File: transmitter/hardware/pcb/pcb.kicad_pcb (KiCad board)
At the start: 2 copper layers, 19.1 x 33 mm, 2 parts, among them P1 digital, P2 analog

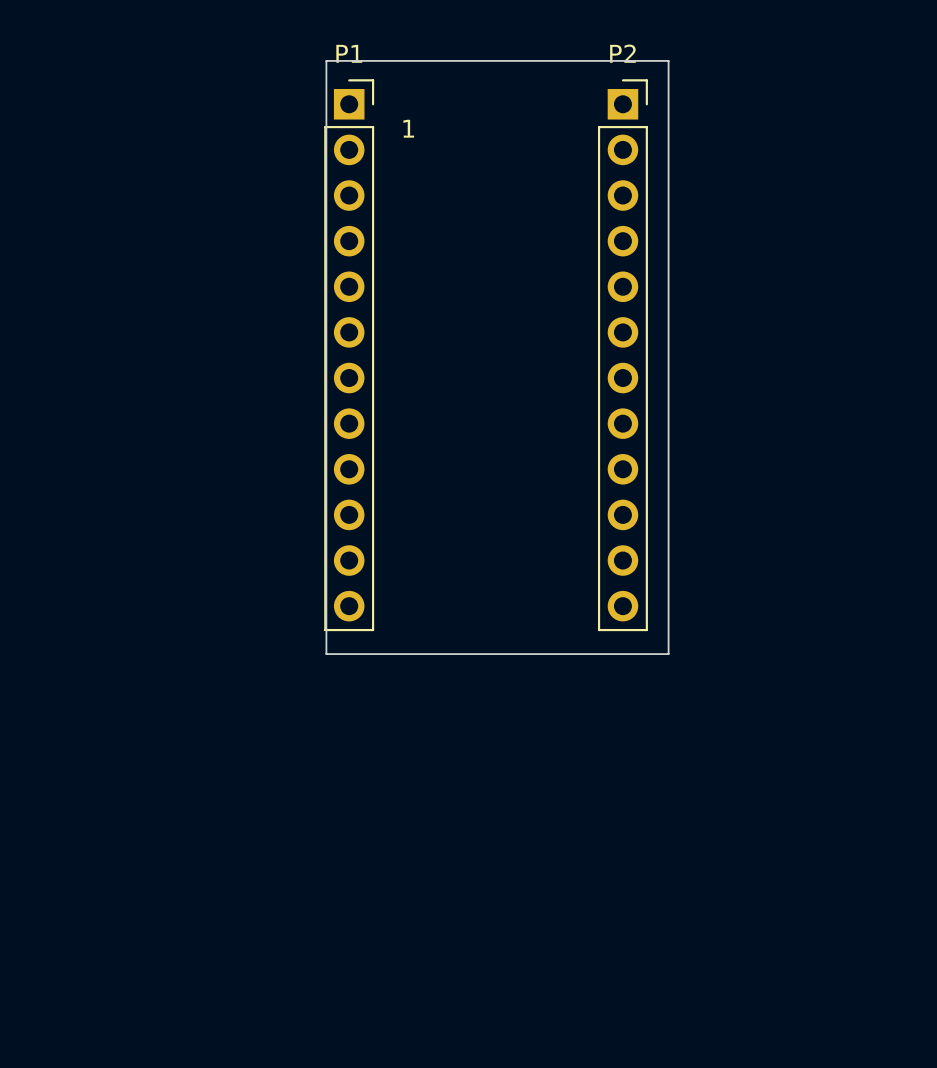
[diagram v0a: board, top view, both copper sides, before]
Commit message: Work on schematics started
Started the work on the schematics for the transmitter part
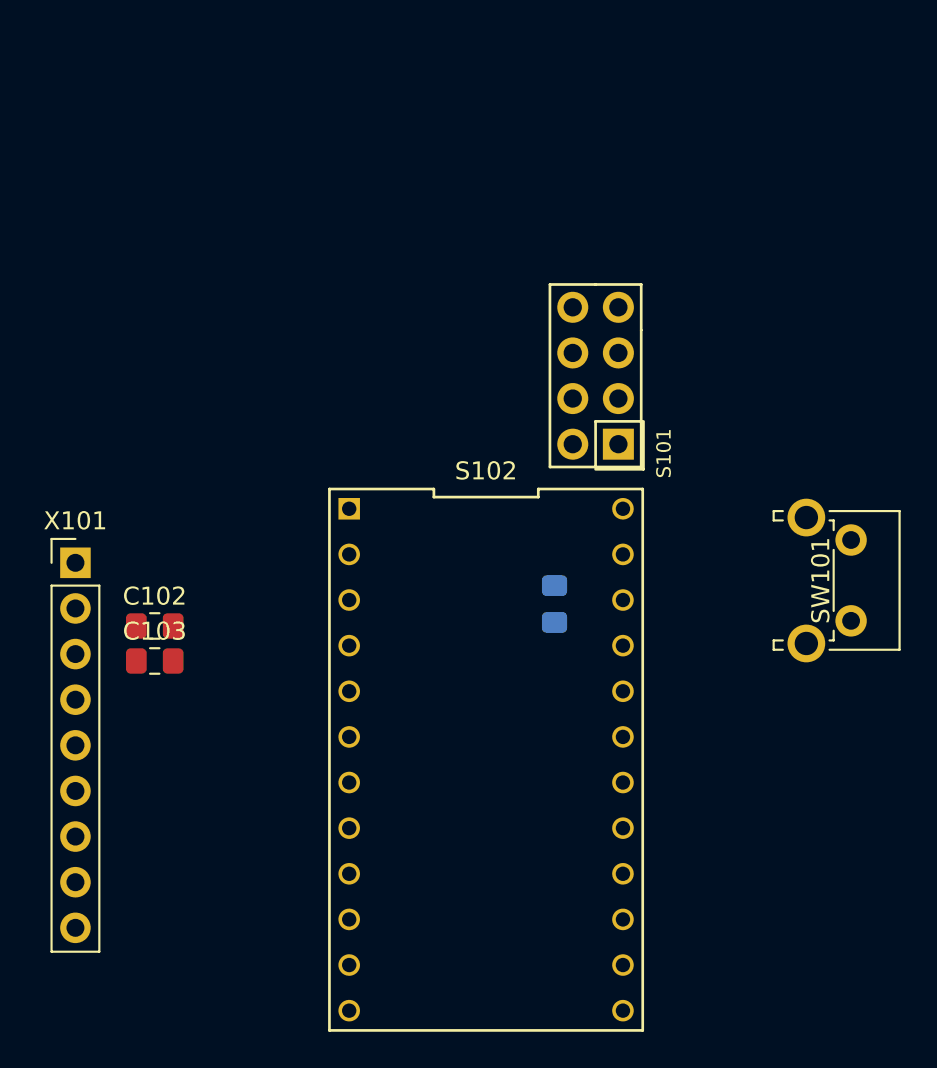
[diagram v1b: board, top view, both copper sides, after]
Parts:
- removed P1: digital, Connector_PinSocket_2.54mm:PinSocket_1x12_P2.54mm_Vertical
- removed P2: analog, Connector_PinSocket_2.54mm:PinSocket_1x12_P2.54mm_Vertical
- added C101: 100n, Capacitor_SMD:C_0805_2012Metric_Pad1.15x1.40mm_HandSolder, B.Cu at (149.9, 97.7)
- added C102: 100n, Capacitor_SMD:C_0805_2012Metric_Pad1.15x1.40mm_HandSolder, F.Cu at (127.6, 98.9)
- added C103: 100n, Capacitor_SMD:C_0805_2012Metric_Pad1.15x1.40mm_HandSolder, F.Cu at (127.6, 100.8)
- added S101: nRF24L01+, Arduino:NRF24L01, F.Cu at (154.9, 90.3)
- added S102: SparkFun_Pro_Micro, Arduino:DIP-24_600, F.Cu at (146.1, 105.5)
- added SW101: ~RST, Button_Switch_THT:SW_Tactile_SPST_Angled_PTS645Vx39-2LFS, F.Cu at (166.4, 94.1)
- added X101: Display, Connector_PinHeader_2.54mm:PinHeader_1x09_P2.54mm_Vertical, F.Cu at (123.2, 95.4)
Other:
- board outline removed
- board text removed: "1"

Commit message: WIP commit
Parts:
- added C104: 100n, Capacitor_SMD:C_0805_2012Metric_Pad1.15x1.40mm_HandSolder, F.Cu at (186.5, 85.7)
- added C105: 10u, Capacitor_SMD:C_1206_3216Metric, F.Cu at (197.7, 71.0)
- added C106: 100n, Capacitor_SMD:C_0805_2012Metric_Pad1.15x1.40mm_HandSolder, F.Cu at (197.3, 73.1)
- added C107: 100n, Capacitor_SMD:C_0805_2012Metric_Pad1.15x1.40mm_HandSolder, F.Cu at (146.9, 100.8)
- added C108: 100n, Capacitor_SMD:C_0805_2012Metric_Pad1.15x1.40mm_HandSolder, F.Cu at (197.3, 75.1)
- added C201: 10n, Capacitor_SMD:C_0603_1608Metric, F.Cu at (226.1, 62.4)
- added C202: 100n, Capacitor_SMD:C_0603_1608Metric, F.Cu at (224.2, 80.8)
- added C203: 15p, Capacitor_SMD:C_0603_1608Metric, F.Cu at (232.4, 80.8)
- added C204: 15p, Capacitor_SMD:C_0603_1608Metric, F.Cu at (226.1, 80.8)
- added C205: 1u, Capacitor_SMD:C_0805_2012Metric_Pad1.15x1.40mm_HandSolder, F.Cu at (219.7, 70.6)
- added C206: 100n, Capacitor_SMD:C_0603_1608Metric, F.Cu at (233.0, 62.4)
- added C207: 100n, Capacitor_SMD:C_0603_1608Metric, F.Cu at (220.3, 67.4)
- added C208: 100n, Capacitor_SMD:C_0603_1608Metric, F.Cu at (224.2, 62.4)
- added C209: 100n, Capacitor_SMD:C_0603_1608Metric, F.Cu at (236.9, 74.4)
- added P101: TestPoint_Alt, TestPoint:TestPoint_Pad_D1.0mm, F.Cu at (185.6, 92.8)
- added P102: TestPoint_Alt, TestPoint:TestPoint_Pad_D1.0mm, F.Cu at (163.0, 90.0)
- added P103: TestPoint_Alt, TestPoint:TestPoint_Pad_D1.0mm, F.Cu at (185.6, 90.7)
- added P104: TestPoint_Alt, TestPoint:TestPoint_Pad_D1.0mm, F.Cu at (192.4, 85.4)
- added P105: TestPoint_Alt, TestPoint:TestPoint_Pad_D1.0mm, F.Cu at (168.9, 90.8)
- added P106: TestPoint_Alt, TestPoint:TestPoint_Pad_D1.0mm, F.Cu at (166.6, 100.0)
- added P107: TestPoint_Alt, TestPoint:TestPoint_Pad_D1.0mm, F.Cu at (166.6, 102.0)
- added P108: TestPoint_Alt, TestPoint:TestPoint_Pad_D1.0mm, F.Cu at (163.0, 94.1)
- added P109: TestPoint_Alt, TestPoint:TestPoint_Pad_D1.0mm, F.Cu at (178.5, 96.9)
- added P110: TestPoint_Alt, TestPoint:TestPoint_Pad_D1.0mm, F.Cu at (189.4, 86.3)
- added P111: TestPoint_Alt, TestPoint:TestPoint_Pad_D1.0mm, F.Cu at (192.4, 83.4)
- added P112: TestPoint_Alt, TestPoint:TestPoint_Pad_D1.0mm, F.Cu at (168.9, 86.7)
- added P113: TestPoint_Alt, TestPoint:TestPoint_Pad_D1.0mm, F.Cu at (166.6, 97.9)
- added P114: TestPoint_Alt, TestPoint:TestPoint_Pad_D1.0mm, F.Cu at (168.9, 88.7)
- added P115: TestPoint_Alt, TestPoint:TestPoint_Pad_D1.0mm, F.Cu at (188.6, 88.3)
- added P116: TestPoint_Alt, TestPoint:TestPoint_Pad_D1.0mm, F.Cu at (196.5, 82.1)
- added P117: TestPoint_Alt, TestPoint:TestPoint_Pad_D1.0mm, F.Cu at (198.2, 80.1)
- added P118: TestPoint_Alt, TestPoint:TestPoint_Pad_D1.0mm, F.Cu at (178.5, 101.0)
- added P119: TestPoint_Alt, TestPoint:TestPoint_Pad_D1.0mm, F.Cu at (181.5, 93.9)
- added P120: TestPoint_Alt, TestPoint:TestPoint_Pad_D1.0mm, F.Cu at (163.0, 92.1)
- added P121: TestPoint_Alt, TestPoint:TestPoint_Pad_D1.0mm, F.Cu at (183.6, 95.5)
- added P122: TestPoint_Alt, TestPoint:TestPoint_Pad_D1.0mm, F.Cu at (180.6, 99.0)
- added P123: TestPoint_Alt, TestPoint:TestPoint_Pad_D1.0mm, F.Cu at (194.4, 85.4)
- added P124: TestPoint_Alt, TestPoint:TestPoint_Pad_D1.0mm, F.Cu at (196.2, 80.1)
- added P125: TestPoint_Alt, TestPoint:TestPoint_Pad_D1.0mm, F.Cu at (183.6, 93.5)
- added P126: TestPoint_Alt, TestPoint:TestPoint_Pad_D1.0mm, F.Cu at (178.5, 99.0)
- added P127: TestPoint_Alt, TestPoint:TestPoint_Pad_D1.0mm, F.Cu at (180.6, 96.9)
- added P128: TestPoint_Alt, TestPoint:TestPoint_Pad_D1.0mm, F.Cu at (194.4, 83.4)
- added P129: TestPoint_Alt, TestPoint:TestPoint_Pad_D1.0mm, F.Cu at (187.7, 90.7)
- added P130: TestPoint_Alt, TestPoint:TestPoint_Pad_D1.0mm, F.Cu at (190.7, 88.3)
- added P131: TestPoint_Alt, TestPoint:TestPoint_Pad_D1.0mm, F.Cu at (213.4, 88.4)
- added P201: TestPoint_Alt, TestPoint:TestPoint_Pad_D1.0mm, F.Cu at (227.3, 62.4)
- added P202: TestPoint_Alt, TestPoint:TestPoint_Pad_D1.0mm, F.Cu at (230.5, 78.9)
- added P203: TestPoint_Alt, TestPoint:TestPoint_Pad_D1.0mm, F.Cu at (228.0, 78.9)
- added P204: TestPoint_Alt, TestPoint:TestPoint_Pad_D1.0mm, F.Cu at (217.8, 71.2)
- added Q101: BC847, Package_TO_SOT_SMD:SOT-23, F.Cu at (159.7, 99.5)
- added Q201: 16M, Crystal:Crystal_SMD_TXC_7M-4Pin_3.2x2.5mm, F.Cu at (229.2, 81.4)
- added R101: 22R, Resistor_SMD:R_0603_1608Metric, F.Cu at (189.9, 84.5)
- added R102: 22R, Resistor_SMD:R_0603_1608Metric, F.Cu at (179.0, 95.2)
- added R103: 2k, Resistor_SMD:R_0603_1608Metric, F.Cu at (182.6, 91.7)
- added R104: 1k, Resistor_SMD:R_0603_1608Metric, F.Cu at (179.0, 93.7)
- added R105: 2.9k, Resistor_SMD:R_0603_1608Metric, F.Cu at (189.8, 83.0)
- added R106: 1k, Resistor_SMD:R_0603_1608Metric, F.Cu at (193.4, 81.6)
- added R107: 330R, Resistor_SMD:R_0603_1608Metric, F.Cu at (197.2, 76.8)
- added R108: 0R, Resistor_SMD:R_0603_1608Metric, F.Cu at (186.1, 87.5)
- added R109: 6.8k, Resistor_SMD:R_0603_1608Metric, F.Cu at (186.1, 89.0)
- added R110: 1.6k, Resistor_SMD:R_0603_1608Metric, F.Cu at (159.5, 102.0)
- added R111: 620R, Resistor_SMD:R_0603_1608Metric, F.Cu at (146.6, 102.6)
- added R112: 150R, Resistor_SMD:R_0603_1608Metric, F.Cu at (197.2, 78.3)
- added R201: 1k, Resistor_SMD:R_0603_1608Metric, F.Cu at (225.4, 78.2)
- added R202: 100R, Resistor_SMD:R_0603_1608Metric, F.Cu at (222.2, 62.4)
- added RN101: 1k, Resistor_THT:R_Array_SIP9, F.Cu at (142.2, 87.3)
- added S103: NRF24L01_Breakout, RF_Module:nRF24L01_Breakout, F.Cu at (142.2, 72.1)
- added S201: ATmega32U4-AU, Package_QFP:TQFP-44_10x10mm_P0.8mm, F.Cu at (228.6, 70.6)
- added U101: AMS1117-3.3, Package_TO_SOT_SMD:SOT-223-3_TabPin2, F.Cu at (153.5, 99.8)
- added X102: SW1, Connector_PinHeader_2.54mm:PinHeader_1x02_P2.54mm_Vertical, F.Cu at (163.8, 98.7)
- added X103: SW2, Connector_PinHeader_2.54mm:PinHeader_1x02_P2.54mm_Vertical, F.Cu at (193.6, 71.7)
- added X104: SW3, Connector_PinHeader_2.54mm:PinHeader_1x02_P2.54mm_Vertical, F.Cu at (179.1, 86.6)
- added X105: SW4, Connector_PinHeader_2.54mm:PinHeader_1x02_P2.54mm_Vertical, F.Cu at (190.1, 77.9)
- added X106: SW5, Connector_PinHeader_2.54mm:PinHeader_1x02_P2.54mm_Vertical, F.Cu at (189.9, 71.7)
- added X107: SW6, Connector_PinHeader_2.54mm:PinHeader_1x02_P2.54mm_Vertical, F.Cu at (182.8, 86.6)
- added X108: SW7, Connector_PinHeader_2.54mm:PinHeader_1x02_P2.54mm_Vertical, F.Cu at (186.4, 80.4)
- added X109: SW8, Connector_PinHeader_2.54mm:PinHeader_1x02_P2.54mm_Vertical, F.Cu at (182.8, 80.4)
- added X110: PWR_5V, Connector_PinHeader_2.54mm:PinHeader_1x02_P2.54mm_Vertical, F.Cu at (179.1, 80.4)
- added X111: UART, Connector_PinHeader_2.54mm:PinHeader_1x04_P2.54mm_Vertical, F.Cu at (166.1, 87.5)
- added X112: gimbal_left_h, Connector_PinSocket_2.54mm:PinSocket_1x03_P2.54mm_Vertical, F.Cu at (179.1, 71.7)
- added X113: gimbal_left_v, Connector_PinSocket_2.54mm:PinSocket_1x03_P2.54mm_Vertical, F.Cu at (182.7, 71.7)
- added X114: gimbal_right_h, Connector_PinSocket_2.54mm:PinSocket_1x03_P2.54mm_Vertical, F.Cu at (186.3, 71.7)
- added X115: gimbal_right_v, Connector_PinSocket_2.54mm:PinSocket_1x03_P2.54mm_Vertical, F.Cu at (160.2, 90.8)
- added X116: analog trimm buttons, Connector_PinHeader_2.54mm:PinHeader_1x09_P2.54mm_Vertical, F.Cu at (171.8, 71.7)
- added X117: Display, Connector_PinHeader_2.54mm:PinHeader_1x09_P2.54mm_Vertical, F.Cu at (175.5, 71.7)
- added X201: AVR-ISP-6, Connector_PinHeader_2.54mm:PinHeader_2x03_P2.54mm_Vertical, F.Cu at (214.6, 75.1)
- C101: value 100n -> 10u; footprint Capacitor_SMD:C_0805_2012Metric_Pad1.15x1.40mm_HandSolder -> Capacitor_SMD:C_1206_3216Metric; moved to F.Cu
- S101: value nRF24L01+ -> 74HC165; footprint Arduino:NRF24L01 -> Package_SO:SOIC-16_3.9x9.9mm_P1.27mm
- S102: value SparkFun_Pro_Micro -> 74AHC1G125; footprint Arduino:DIP-24_600 -> Package_TO_SOT_SMD:SOT-353_SC-70-5
- X101: value Display -> USB_B_Micro; footprint Connector_PinHeader_2.54mm:PinHeader_1x09_P2.54mm_Vertical -> Connector_USB:USB_Micro-B_GCT_USB3076-30-A
- moved C103 70.3 mm to (193.8, 77.0)
- moved S102 54.2 mm to (193.5, 79.4)
- moved C102 52.1 mm to (179.2, 91.9)
- moved X101 30.8 mm to (153.7, 91.7)
- moved S101 11.0 mm to (144.8, 94.4), turned to 0 degrees
- moved C101 7.83 mm to (142.8, 101.0), turned to 0 degrees
- moved SW101 5.43 mm to (170.4, 97.7), turned to 0 degrees
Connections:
- C102 pad 1: +3V3 -> +5V
- S101 pad 1: GND -> /PE_LATCH
- S101 pad 2: +3V3 -> /SCK
- S101 pad 3: /CE -> Net-(P105-Pad1)
- S101 pad 4: /~CS1 -> Net-(P106-Pad1)
- S101 pad 5: /SCK -> Net-(P107-Pad1)
- S101 pad 6: /MOSI -> Net-(P108-Pad1)
- S101 pad 7: /MISO -> Net-(S101-Pad7)
- S101 pad 8: /IRQ -> GND
- S102 pad 1: /~RST -> /~CE3
- S102 pad 2: /BLEN -> Net-(P116-Pad1)
- S102 pad 4: GND -> /MISO
- S102 pad 5: /IRQ -> +5V
- SW101 pad 1: GND -> /~RST
- SW101 pad 2: Net-(S102-Pad22) -> GND
- X101 pad 1: GND -> /VBUS
- X101 pad 2: +5V -> Net-(R102-Pad2)
- X101 pad 3: /~RST -> Net-(R101-Pad2)
- X101 pad 4: /DC -> Net-(X101-Pad4)
- X101 pad 5: /MOSI -> GND
- X101 pad 6: /SCK -> GND
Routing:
- net GND: track 0.00 -> 31.9 mm
- net /MOSI: track 0.00 -> 11.3 mm
- net /SCK: track 0.00 -> 8.48 mm
- net /MISO: track 0.00 -> 8.45 mm
- net Net-(C208-Pad1): track 0.00 -> 8.26 mm
- net Net-(C203-Pad1): track 0.00 -> 7.62 mm
- net Net-(C204-Pad1): track 0.00 -> 6.70 mm
- net Net-(C205-Pad1): track 0.00 -> 5.68 mm
- net +5V: track 0.00 -> 5.65 mm
- net /~RST: track 0.00 -> 4.19 mm
- net Net-(C201-Pad1): track 0.00 -> 3.42 mm

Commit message: WIP
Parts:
- added C109: 10u, Capacitor_SMD:C_1206_3216Metric, F.Cu at (167.4, 89.0)
- added C110: 10u, Capacitor_SMD:C_1206_3216Metric, F.Cu at (182.9, 97.7)
- added C111: 10u, Capacitor_SMD:C_1206_3216Metric, F.Cu at (123.6, 81.6)
- added C112: 100n, Capacitor_SMD:C_0805_2012Metric_Pad1.15x1.40mm_HandSolder, F.Cu at (127.8, 83.4)
- added C113: 100n, Capacitor_SMD:C_0805_2012Metric_Pad1.15x1.40mm_HandSolder, F.Cu at (127.8, 81.4)
- added C114: 100n, Capacitor_SMD:C_0805_2012Metric_Pad1.15x1.40mm_HandSolder, F.Cu at (123.2, 83.7)
- added D101: green, LED_THT:LED_D3.0mm, F.Cu at (239.7, 102.2)
- added D102: red, LED_THT:LED_D3.0mm, F.Cu at (235.3, 102.2)
- added P132: TestPoint_Alt, TestPoint:TestPoint_Pad_D1.0mm, F.Cu at (201.3, 86.4)
- added P133: TestPoint_Alt, TestPoint:TestPoint_Pad_D1.0mm, F.Cu at (192.4, 94.2)
- added P134: TestPoint_Alt, TestPoint:TestPoint_Pad_D1.0mm, F.Cu at (198.2, 87.9)
- added P135: TestPoint_Alt, TestPoint:TestPoint_Pad_D1.0mm, F.Cu at (184.1, 99.7)
- added P136: TestPoint_Alt, TestPoint:TestPoint_Pad_D1.0mm, F.Cu at (195.2, 90.5)
- added P137: TestPoint_Alt, TestPoint:TestPoint_Pad_D1.0mm, F.Cu at (211.5, 74.7)
- added P138: TestPoint_Alt, TestPoint:TestPoint_Pad_D1.0mm, F.Cu at (174.6, 83.5)
- added P139: TestPoint_Alt, TestPoint:TestPoint_Pad_D1.0mm, F.Cu at (119.9, 85.8)
- added P140: TestPoint_Alt, TestPoint:TestPoint_Pad_D1.0mm, F.Cu at (117.9, 87.9)
- added P141: TestPoint_Alt, TestPoint:TestPoint_Pad_D1.0mm, F.Cu at (117.9, 85.8)
- added P142: TestPoint_Alt, TestPoint:TestPoint_Pad_D1.0mm, F.Cu at (119.9, 87.9)
- added P143: TestPoint_Alt, TestPoint:TestPoint_Pad_D1.0mm, F.Cu at (122.0, 87.2)
- added P144: TestPoint_Alt, TestPoint:TestPoint_Pad_D1.0mm, F.Cu at (114.9, 89.9)
- added P145: TestPoint_Alt, TestPoint:TestPoint_Pad_D1.0mm, F.Cu at (116.9, 89.9)
- added R113: 1.6k, Resistor_SMD:R_0603_1608Metric, F.Cu at (189.9, 91.9)
- added R114: 1k, Resistor_SMD:R_0603_1608Metric, F.Cu at (195.7, 85.7)
- added R115: 620R, Resistor_SMD:R_0603_1608Metric, F.Cu at (195.7, 88.7)
- added R116: 330R, Resistor_SMD:R_0603_1608Metric, F.Cu at (202.6, 79.9)
- added R117: 150R, Resistor_SMD:R_0603_1608Metric, F.Cu at (181.6, 101.4)
- added R118: 0R, Resistor_SMD:R_0603_1608Metric, F.Cu at (115.3, 87.0)
- added R119: 1k, Resistor_SMD:R_0603_1608Metric, F.Cu at (122.8, 85.5)
- added S104: 74AHC1G125, Package_TO_SOT_SMD:SOT-353_SC-70-5, F.Cu at (177.3, 93.8)
- added S105: 74HC165, Package_SO:SOIC-16_3.9x9.9mm_P1.27mm, F.Cu at (117.6, 79.5)
- added SW102: ~RST, Button_Switch_THT:SW_Tactile_SPST_Angled_PTS645Vx39-2LFS, F.Cu at (201.6, 68.5)
- added X118: analog_in1, Connector_Molex:Molex_KK-254_AE-6410-05A_1x05_P2.54mm_Vertical, F.Cu at (144.5, 126.3)
- added X119: SW5, Connector_PinHeader_2.54mm:PinHeader_1x02_P2.54mm_Vertical, F.Cu at (126.8, 76.1)
- added X120: SW6, Connector_PinHeader_2.54mm:PinHeader_1x02_P2.54mm_Vertical, F.Cu at (123.1, 76.1)
- added X121: SW7, Connector_PinHeader_2.54mm:PinHeader_1x02_P2.54mm_Vertical, F.Cu at (134.1, 76.1)
- added X122: analog trimm buttons, Connector_PinHeader_2.54mm:PinHeader_1x09_P2.54mm_Vertical, F.Cu at (112.0, 76.1)
- added X123: SW8, Connector_PinHeader_2.54mm:PinHeader_1x02_P2.54mm_Vertical, F.Cu at (130.4, 76.1)
- C104, C106: value 100n -> 10u; footprint Capacitor_SMD:C_0805_2012Metric_Pad1.15x1.40mm_HandSolder -> Capacitor_SMD:C_1206_3216Metric
- C105: value 10u -> 100n; footprint Capacitor_SMD:C_1206_3216Metric -> Capacitor_SMD:C_0805_2012Metric_Pad1.15x1.40mm_HandSolder; moved to B.Cu
- C201: value 10n -> 100n
- C203, C204: value 15p -> 100n
- C205: value 1u -> 100n; footprint Capacitor_SMD:C_0805_2012Metric_Pad1.15x1.40mm_HandSolder -> Capacitor_SMD:C_0603_1608Metric
- C206, C207: value 100n -> 15p
- C208: value 100n -> 10n
- C209: value 100n -> 1u; footprint Capacitor_SMD:C_0603_1608Metric -> Capacitor_SMD:C_0805_2012Metric_Pad1.15x1.40mm_HandSolder
- Q201: footprint Crystal:Crystal_SMD_TXC_7M-4Pin_3.2x2.5mm -> Crystal:Crystal_SMD_HC49-SD
- R101: value 22R -> n.b
- R102: value 22R -> 1k
- R103: value 2k -> 1k
- R104: value 1k -> 1,2k
- R105: value 2.9k -> 0R
- R106: value 1k -> 4,7k
- R107: value 330R -> 4,7k
- R108: value 0R -> 22R
- R109: value 6.8k -> 22R
- R110: value 1.6k -> 2k
- R111: value 620R -> 6.8k
- R112: value 150R -> 2.9k
- R201: value 1k -> 100R
- R202: value 100R -> 1k
- S101: value 74HC165 -> Step-Up; footprint Package_SO:SOIC-16_3.9x9.9mm_P1.27mm -> Package_SO:SOIC-8-1EP_3.9x4.9mm_P1.27mm_EP2.35x2.35mm
- S102: value 74AHC1G125 -> NRF24L01_Breakout; footprint Package_TO_SOT_SMD:SOT-353_SC-70-5 -> RF_Module:nRF24L01_Breakout
- S103: value NRF24L01_Breakout -> TP4056; footprint RF_Module:nRF24L01_Breakout -> Package_SO:SOIC-8-1EP_3.9x4.9mm_P1.27mm_EP2.35x2.35mm
- SW101: value ~RST -> Power; footprint Button_Switch_THT:SW_Tactile_SPST_Angled_PTS645Vx39-2LFS -> Module:SW_Graupner_JS202011AQN_DPDT_Angled
- X101: value USB_B_Micro -> PWR_5V; footprint Connector_USB:USB_Micro-B_GCT_USB3076-30-A -> Connector_PinHeader_2.54mm:PinHeader_1x03_P2.54mm_Vertical
- X102: value SW1 -> Charger; footprint Connector_PinHeader_2.54mm:PinHeader_1x02_P2.54mm_Vertical -> Connector_BarrelJack:BarrelJack_Horizontal
- X103: value SW2 -> Display; footprint Connector_PinHeader_2.54mm:PinHeader_1x02_P2.54mm_Vertical -> Connector_PinHeader_2.54mm:PinHeader_1x09_P2.54mm_Vertical
- X104: value SW3 -> I2C; footprint Connector_PinHeader_2.54mm:PinHeader_1x02_P2.54mm_Vertical -> Connector_PinHeader_2.54mm:PinHeader_1x04_P2.54mm_Vertical
- X105: value SW4 -> UART; footprint Connector_PinHeader_2.54mm:PinHeader_1x02_P2.54mm_Vertical -> Connector_PinHeader_2.54mm:PinHeader_1x04_P2.54mm_Vertical
- X106: value SW5 -> USB_B_Micro; footprint Connector_PinHeader_2.54mm:PinHeader_1x02_P2.54mm_Vertical -> Connector_USB:USB_Micro-B_GCT_USB3076-30-A
- X107: value SW6 -> analog_in2; footprint Connector_PinHeader_2.54mm:PinHeader_1x02_P2.54mm_Vertical -> Connector_Molex:Molex_KK-254_AE-6410-05A_1x05_P2.54mm_Vertical
- X108: value SW7 -> analog_in3; footprint Connector_PinHeader_2.54mm:PinHeader_1x02_P2.54mm_Vertical -> Connector_Molex:Molex_KK-254_AE-6410-05A_1x05_P2.54mm_Vertical
- X109: value SW8 -> gimbal_left_h; footprint Connector_PinHeader_2.54mm:PinHeader_1x02_P2.54mm_Vertical -> Connector_Molex:Molex_KK-254_AE-6410-05A_1x05_P2.54mm_Vertical
- X110: value PWR_5V -> analog_in4; footprint Connector_PinHeader_2.54mm:PinHeader_1x02_P2.54mm_Vertical -> Connector_Molex:Molex_KK-254_AE-6410-05A_1x05_P2.54mm_Vertical
- X111: value UART -> gimbal_left_v; footprint Connector_PinHeader_2.54mm:PinHeader_1x04_P2.54mm_Vertical -> Connector_Molex:Molex_KK-254_AE-6410-05A_1x05_P2.54mm_Vertical
- X112: value gimbal_left_h -> gimbal_right_h; footprint Connector_PinSocket_2.54mm:PinSocket_1x03_P2.54mm_Vertical -> Connector_Molex:Molex_KK-254_AE-6410-05A_1x05_P2.54mm_Vertical
- X113: value gimbal_left_v -> SW1; footprint Connector_PinSocket_2.54mm:PinSocket_1x03_P2.54mm_Vertical -> Connector_PinHeader_2.54mm:PinHeader_1x02_P2.54mm_Vertical
- X114: value gimbal_right_h -> SW2; footprint Connector_PinSocket_2.54mm:PinSocket_1x03_P2.54mm_Vertical -> Connector_PinHeader_2.54mm:PinHeader_1x02_P2.54mm_Vertical
- X115: footprint Connector_PinSocket_2.54mm:PinSocket_1x03_P2.54mm_Vertical -> Connector_Molex:Molex_KK-254_AE-6410-05A_1x05_P2.54mm_Vertical
- X116: value analog trimm buttons -> SW3; footprint Connector_PinHeader_2.54mm:PinHeader_1x09_P2.54mm_Vertical -> Connector_PinHeader_2.54mm:PinHeader_1x02_P2.54mm_Vertical
- X117: value Display -> SW4; footprint Connector_PinHeader_2.54mm:PinHeader_1x09_P2.54mm_Vertical -> Connector_PinHeader_2.54mm:PinHeader_1x02_P2.54mm_Vertical
- moved S102 114.0 mm to (95.6, 137.8), turned to 180 degrees
- moved S101 85.7 mm to (229.6, 106.6)
- moved P108 76.5 mm to (238.5, 106.6)
- moved C105 75.7 mm to (219.4, 143.5)
- moved X101 68.4 mm to (213.1, 125.7)
- moved S103 68.0 mm to (210.3, 72.2)
- moved P106 67.6 mm to (234.0, 106.0)
- moved X102 66.4 mm to (216.2, 139.6), turned to 180 degrees
- moved P105 64.7 mm to (211.4, 139.5)
- moved R102 61.5 mm to (239.7, 104.7), turned to 270 degrees
- moved SW101 59.5 mm to (195.7, 151.6), turned to 180 degrees
- moved X112 58.9 mm to (157.2, 126.3), turned to 90 degrees
- moved C106 56.5 mm to (209.9, 128.2), turned to 270 degrees
- moved R103 54.3 mm to (235.3, 104.7), turned to 270 degrees
- moved P113 48.8 mm to (211.5, 78.8)
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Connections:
- C103 pad 1: +5V -> +3V3
- C106 pad 1: +5V -> Net-(C106-Pad1)
- C107 pad 1: +3V3 -> Net-(C106-Pad1)
- C201 pad 1: Net-(C201-Pad1) -> +5V
- C202 pad 1: /~RST -> +5V
- C204 pad 1: Net-(C204-Pad1) -> Net-(C203-Pad1)
- C205 pad 1: Net-(C205-Pad1) -> /~RST
- C206 pad 1: +5V -> Net-(C206-Pad1)
- C207 pad 1: +5V -> Net-(C207-Pad1)
- C209 pad 1: Net-(C208-Pad1) -> Net-(C209-Pad1)
- P101 pad 1: Net-(P101-Pad1) -> +3V3
- P102 pad 1: Net-(P102-Pad1) -> Net-(C106-Pad1)
- P103 pad 1: Net-(P103-Pad1) -> +BATT
- P104 pad 1: Net-(P104-Pad1) -> GND
- P105 pad 1: Net-(P105-Pad1) -> ~CS_nRF24
- P106 pad 1: Net-(P106-Pad1) -> CE
- P107 pad 1: Net-(P107-Pad1) -> +5C
- P109 pad 1: GND -> /NTC
- P110 pad 1: +5V -> Net-(P110-Pad1)
- P111 pad 1: /~RST -> Net-(P111-Pad1)
- P112 pad 1: /VBUS -> ~LCD_RST
- P113 pad 1: /microcontroller/D- -> LCD_DC
- P114 pad 1: /microcontroller/D+ -> MOSI
- P115 pad 1: +3V3 -> SCK
- P116 pad 1: Net-(P116-Pad1) -> ~CS_LCD
- P117 pad 1: /TX -> LCD_BL
- P118 pad 1: /RX -> /SCL
- P119 pad 1: /CE -> /SDA
- P120 pad 1: /~CS1 -> /~RST
- P121 pad 1: /IRQ -> /RX
- P122 pad 1: /GIMBAL_LEFT_H -> /TX
- P123 pad 1: /GIMBAL_LEFT_V -> /VBUS
- P124 pad 1: /GIMBAL_RIGHT_H -> /microcontroller/D+
- P125 pad 1: /GIMBAL_RIGHT_V -> /microcontroller/D-
- P126 pad 1: /~LCD_RST -> /ANALOG_CH2
- P127 pad 1: /MOSI -> /ANALOG_CH3
- P128 pad 1: /~LCD_CS -> /GIMBAL_LEFT_H
- P129 pad 1: /LCD_DC -> /ANALOG_CH4
- P130 pad 1: /SCK -> /GIMBAL_LEFT_V
- P131 pad 1: /LCD_BL -> /GIMBAL_RIGHT_H
- P201 pad 1: Net-(C201-Pad1) -> Net-(C206-Pad1)
- P202 pad 1: Net-(C203-Pad1) -> Net-(C207-Pad1)
- P203 pad 1: Net-(C204-Pad1) -> Net-(C208-Pad1)
- P204 pad 1: Net-(C205-Pad1) -> Net-(C209-Pad1)
- Q101 pad 1: /LCD_BL -> LCD_BL
- Q201 pad 1: Net-(C203-Pad1) -> Net-(C206-Pad1)
- Q201 pad 2: Net-(C204-Pad1) -> Net-(C207-Pad1)
- R101 pad 1: /microcontroller/D+ -> +5C
- R101 pad 2: Net-(R101-Pad2) -> /NTC
- R102 pad 1: /microcontroller/D- -> Net-(D101-Pad1)
- R102 pad 2: Net-(R102-Pad2) -> Net-(P110-Pad1)
- R103 pad 1: /MISO -> Net-(D102-Pad1)
- R103 pad 2: Net-(P116-Pad1) -> Net-(P108-Pad1)
- R104 pad 1: /AN_TRIM_BUTTONS -> Net-(P111-Pad1)
- R105 pad 1: /AN_TRIM_BUTTONS -> /NTC
- R105 pad 2: Net-(R105-Pad2) -> GND
- R106 pad 1: /AN_TRIM_BUTTONS -> +5V
- R106 pad 2: Net-(R106-Pad2) -> /SDA
- R107 pad 1: /AN_TRIM_BUTTONS -> +5V
- R107 pad 2: Net-(R107-Pad2) -> /SCL
- R108 pad 1: /AN_TRIM_BUTTONS -> /microcontroller/D+
- R109 pad 1: /AN_TRIM_BUTTONS -> /microcontroller/D-
- R110 pad 1: /AN_TRIM_BUTTONS -> MISO
- R110 pad 2: Net-(R110-Pad2) -> Net-(P136-Pad1)
- R201 pad 2: /~RST -> Net-(C203-Pad1)
- R202 pad 2: Net-(C208-Pad1) -> /~RST
- RN101 pad 2: Net-(P101-Pad1) -> Net-(P132-Pad1)
- RN101 pad 3: Net-(P102-Pad1) -> Net-(P133-Pad1)
- RN101 pad 4: Net-(P103-Pad1) -> Net-(P135-Pad1)
- RN101 pad 5: Net-(P104-Pad1) -> Net-(P137-Pad1)
- RN101 pad 6: Net-(P105-Pad1) -> Net-(P139-Pad1)
- RN101 pad 7: Net-(P106-Pad1) -> Net-(P140-Pad1)
- RN101 pad 8: Net-(P107-Pad1) -> Net-(P143-Pad1)
- RN101 pad 9: Net-(P108-Pad1) -> Net-(P145-Pad1)
- S101 pad 1: /PE_LATCH -> Net-(C106-Pad1)
- S101 pad 2: /SCK -> GND
- S101 pad 3: Net-(P105-Pad1) -> +5V
- S101 pad 4: Net-(P106-Pad1) -> GND
- S101 pad 5: Net-(P107-Pad1) -> (no net)
- S101 pad 6: Net-(P108-Pad1) -> (no net)
- S101 pad 7: Net-(S101-Pad7) -> (no net)
- S101 pad 8: GND -> (no net)
- S101 pad 9: Net-(P116-Pad1) -> (no net)
- S102 pad 1: /~CE3 -> GND
- S102 pad 2: Net-(P116-Pad1) -> +3V3
- S102 pad 3: GND -> CE
- S102 pad 4: /MISO -> ~CS_nRF24
- S102 pad 5: +5V -> SCK
- S103 pad 1: GND -> /NTC
- S103 pad 2: +3V3 -> Net-(P111-Pad1)
- S103 pad 3: /CE -> GND
- S103 pad 4: /~CS1 -> +5C
- S103 pad 5: /SCK -> +BATT
- S103 pad 6: /MOSI -> Net-(P110-Pad1)
- S103 pad 7: /MISO -> Net-(P108-Pad1)
- S103 pad 8: /IRQ -> +5C
- S201 pad 1: /LCD_BL -> LCD_BL
- S201 pad 10: /MOSI -> MOSI
- S201 pad 11: /MISO -> MISO
- S201 pad 12: /~PE_CS -> ~CS_PE
- S201 pad 16: Net-(C204-Pad1) -> Net-(C207-Pad1)
- S201 pad 17: Net-(C203-Pad1) -> Net-(C206-Pad1)
- S201 pad 18: /~LCD_RST -> /SCL
- S201 pad 19: /microcontroller/PD1\~INT1~\SDA -> /SDA
- S201 pad 22: /microcontroller/PD5\XCK1\~CTS -> ~LCD_RST
- S201 pad 24: Net-(C208-Pad1) -> Net-(C203-Pad1)
- S201 pad 25: /microcontroller/PD4\ICP1\ADC8 -> /ANALOG_CH2
- S201 pad 26: /microcontroller/PD6\T1\~OC4D~\ADC9 -> /ANALOG_CH3
- S201 pad 27: /microcontroller/PD7\T0\OC4D\ADC10 -> /ANALOG_CH4
- S201 pad 28: /CE -> CE
- S201 pad 29: /IRQ -> /microcontroller/PB5\OC1A\PCINT5\~OC4B~\ADC12
- S201 pad 30: /PE_LATCH -> PE_LATCH
- S201 pad 31: /LCD_DC -> LCD_DC
- S201 pad 32: /~LCD_CS -> ~CS_LCD
- S201 pad 36: /microcontroller/PF7\ADC7\TDI -> /AN_TRIM_BUTTONS
- S201 pad 37: /AN_TRIM_BUTTONS -> /ANALOG_CH1
- S201 pad 42: Net-(C201-Pad1) -> Net-(C208-Pad1)
- S201 pad 44: Net-(C208-Pad1) -> Net-(C203-Pad1)
- S201 pad 6: Net-(C205-Pad1) -> Net-(C209-Pad1)
- S201 pad 8: /~CS1 -> ~CS_nRF24
- S201 pad 9: /SCK -> SCK
- SW101 pad 1: /~RST -> Net-(C106-Pad1)
- SW101 pad 2: GND -> +BATT
- X101 pad 1: /VBUS -> +BATT
- X101 pad 2: Net-(R102-Pad2) -> /NTC
- X101 pad 3: Net-(R101-Pad2) -> GND
- X102 pad 1: Net-(P101-Pad1) -> +5C
- X103 pad 1: Net-(P102-Pad1) -> GND
- X103 pad 2: GND -> +5V
- X104 pad 1: Net-(P103-Pad1) -> +5V
- X104 pad 2: GND -> /SCL
- X105 pad 1: Net-(P104-Pad1) -> +5V
- X105 pad 2: GND -> /RX
- X106 pad 1: Net-(P105-Pad1) -> /VBUS
- X106 pad 2: GND -> Net-(R109-Pad2)
- X107 pad 1: Net-(P106-Pad1) -> +5V
- X107 pad 2: GND -> Net-(X107-Pad2)
- X108 pad 1: Net-(P107-Pad1) -> +5V
- X108 pad 2: GND -> Net-(X108-Pad2)
- X109 pad 1: Net-(P108-Pad1) -> +5V
- X109 pad 2: GND -> Net-(X109-Pad2)
- X110 pad 2: GND -> Net-(X110-Pad2)
- X111 pad 2: /RX -> Net-(X111-Pad2)
- X111 pad 3: /TX -> /GIMBAL_LEFT_V
- X111 pad 4: GND -> Net-(X111-Pad4)
- X112 pad 2: /GIMBAL_LEFT_H -> Net-(X112-Pad2)
- X112 pad 3: GND -> /GIMBAL_RIGHT_H
- X113 pad 1: +5V -> Net-(P132-Pad1)
- X113 pad 2: /GIMBAL_LEFT_V -> GND
- X114 pad 1: +5V -> Net-(P133-Pad1)
- X114 pad 2: /GIMBAL_RIGHT_H -> GND
- X115 pad 2: /GIMBAL_RIGHT_V -> Net-(X115-Pad2)
- X115 pad 3: GND -> /GIMBAL_RIGHT_V
- X116 pad 1: +5V -> Net-(P135-Pad1)
- X116 pad 2: Net-(R109-Pad2) -> GND
- X117 pad 1: GND -> Net-(P137-Pad1)
- X117 pad 2: +5V -> GND
- X201 pad 1: /MISO -> MISO
- X201 pad 3: /SCK -> SCK
- X201 pad 4: /MOSI -> MOSI
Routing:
- net GND: track 31.9 -> 0.00 mm
- net /MOSI: track 11.3 -> 0.00 mm
- net /SCK: track 8.48 -> 0.00 mm
- net /MISO: track 8.45 -> 0.00 mm
- net Net-(C208-Pad1): track 8.26 -> 0.00 mm
- net Net-(C203-Pad1): track 7.62 -> 0.00 mm
- net Net-(C204-Pad1): track 6.70 -> 0.00 mm
- net Net-(C205-Pad1): track 5.68 -> 0.00 mm
- net +5V: track 5.65 -> 0.00 mm
- net /~RST: track 4.19 -> 0.00 mm
- net Net-(C201-Pad1): track 3.42 -> 0.00 mm
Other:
- board outline added: 192.5 x 47 mm
